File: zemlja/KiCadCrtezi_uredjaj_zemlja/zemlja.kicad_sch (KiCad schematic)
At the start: 24 parts, among them J1 AVR-ISP-6, J2 Barrel_Jack, J3 Arduino_ESP_Pin_Head_03x04, J4 Arduino_Analog_01x06_Socket, J5 Arduino_Pow_01x08_Socket, J6 Arduino_Pow_01x08_Socket, J7 Arduino_Digital_2_01x10_Socket, SW1 SW_Push, U1 TTL-RS485 Converter, U2 LCD 2x16 I2C, U3 7 in 1 Soil Sensor, U4 L7808

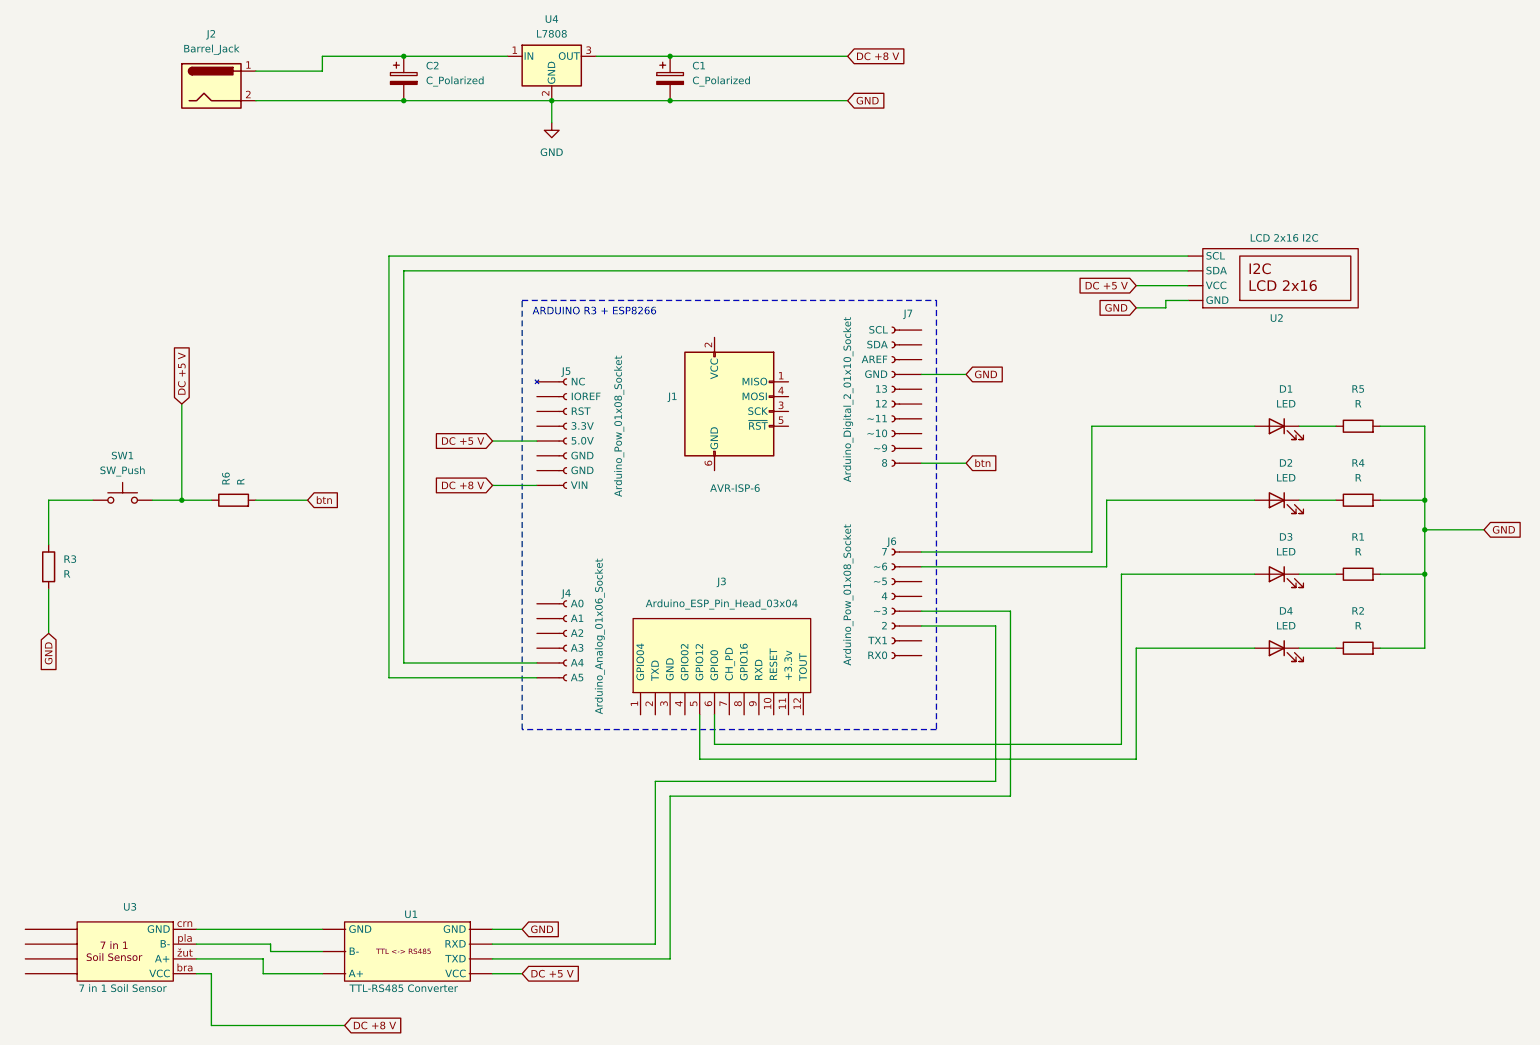
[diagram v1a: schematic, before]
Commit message: Na šemi uredđaja "zemlja" popravljene veze između kontrolnog dugmeta i uređaja. Popravljena i šema povezivanja dugmeta.
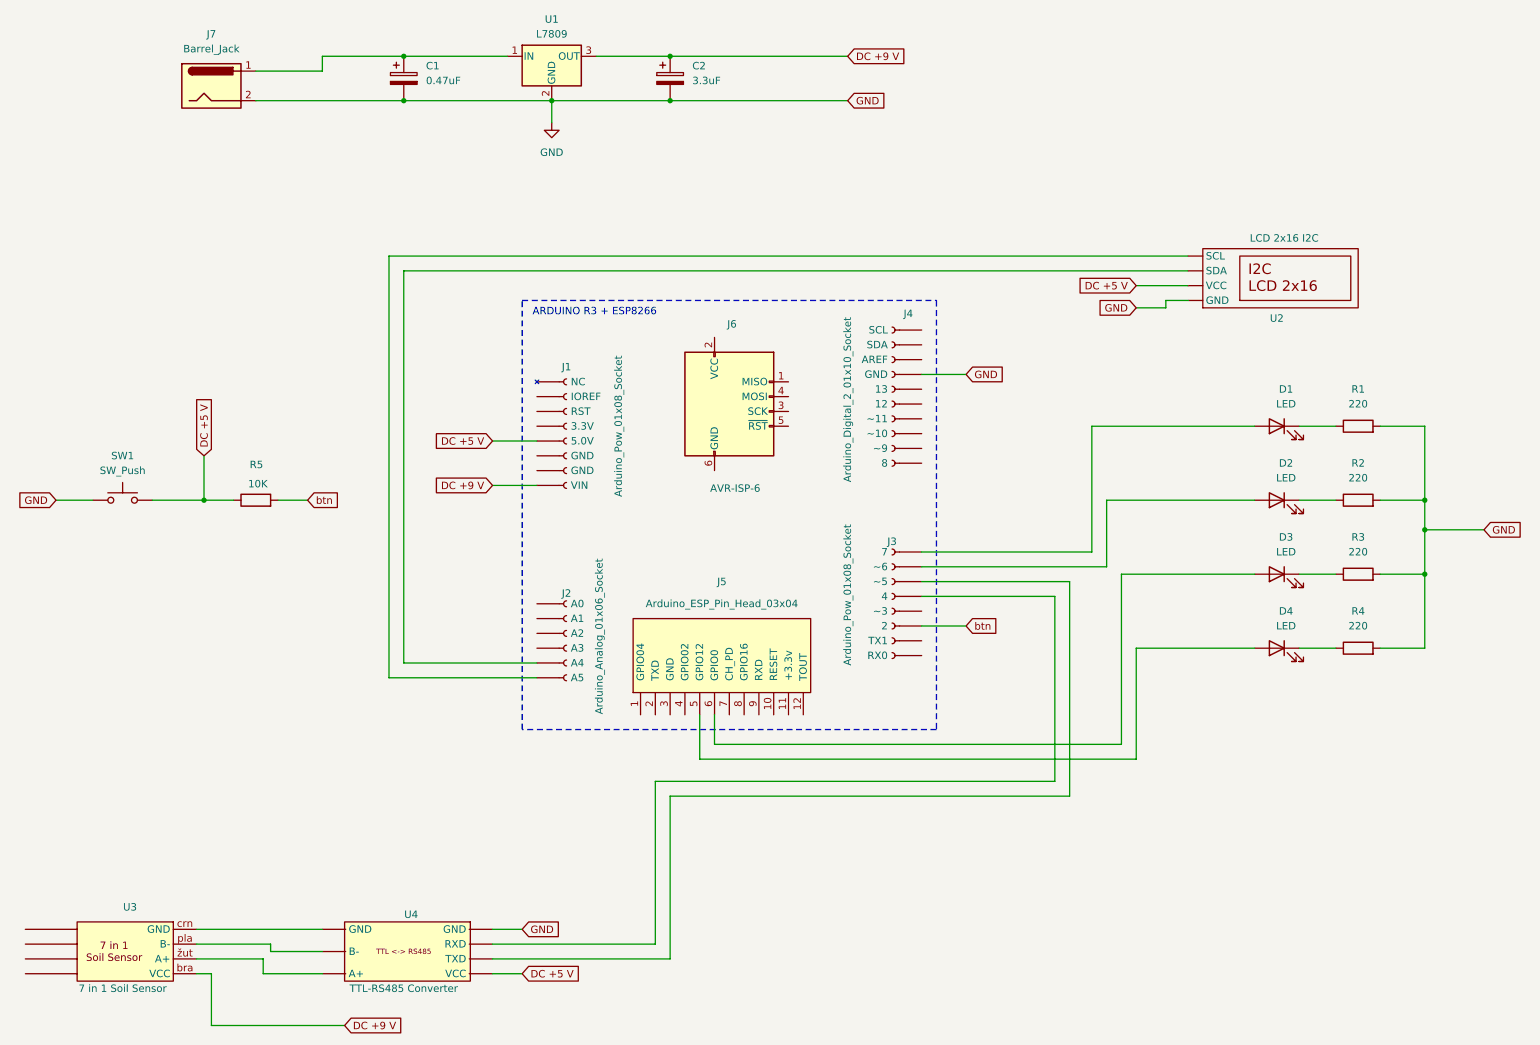
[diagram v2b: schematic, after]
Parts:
- removed R3: R, symbol Device:R
- removed U4: L7808, symbol Regulator_Linear:L7808
- added U1: L7809, symbol Regulator_Linear:L7809
- C1: renamed from C2; value C_Polarized -> 0.47uF
- C2: renamed from C1; value C_Polarized -> 3.3uF
- R1: renamed from R5; value R -> 220
- R2: renamed from R4; value R -> 220
- R3: renamed from R1; value R -> 220
- R4: renamed from R2; value R -> 220
- R5: renamed from R6; value R -> 10K
- renumbered J5 to J1, J4 to J2, J6 to J3, J7 to J4, J3 to J5, J1 to J6, J2 to J7, U1 to U4
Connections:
- net GND: now also SW1.1, U1.2 (GND)
- net btn: now also J3.6 (2); no longer J4.10 (8)
- net at C1.1, J7.1: now also U1.1 (IN)
- net at J3.3 (~5): now also U4. (VCC)
- net at J3.4: now also U4. (VCC)
- net at J3.5 (~3): no longer U4. (VCC)
- net DC +8 V renamed DC +9 V
- net DC +9 V: now also U1.3 (OUT)
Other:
- moved on the sheet: R5

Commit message: Na šemi uređaja zemla popravljene sve veze između led dioda i Arduino. Označene led diode po bojama.
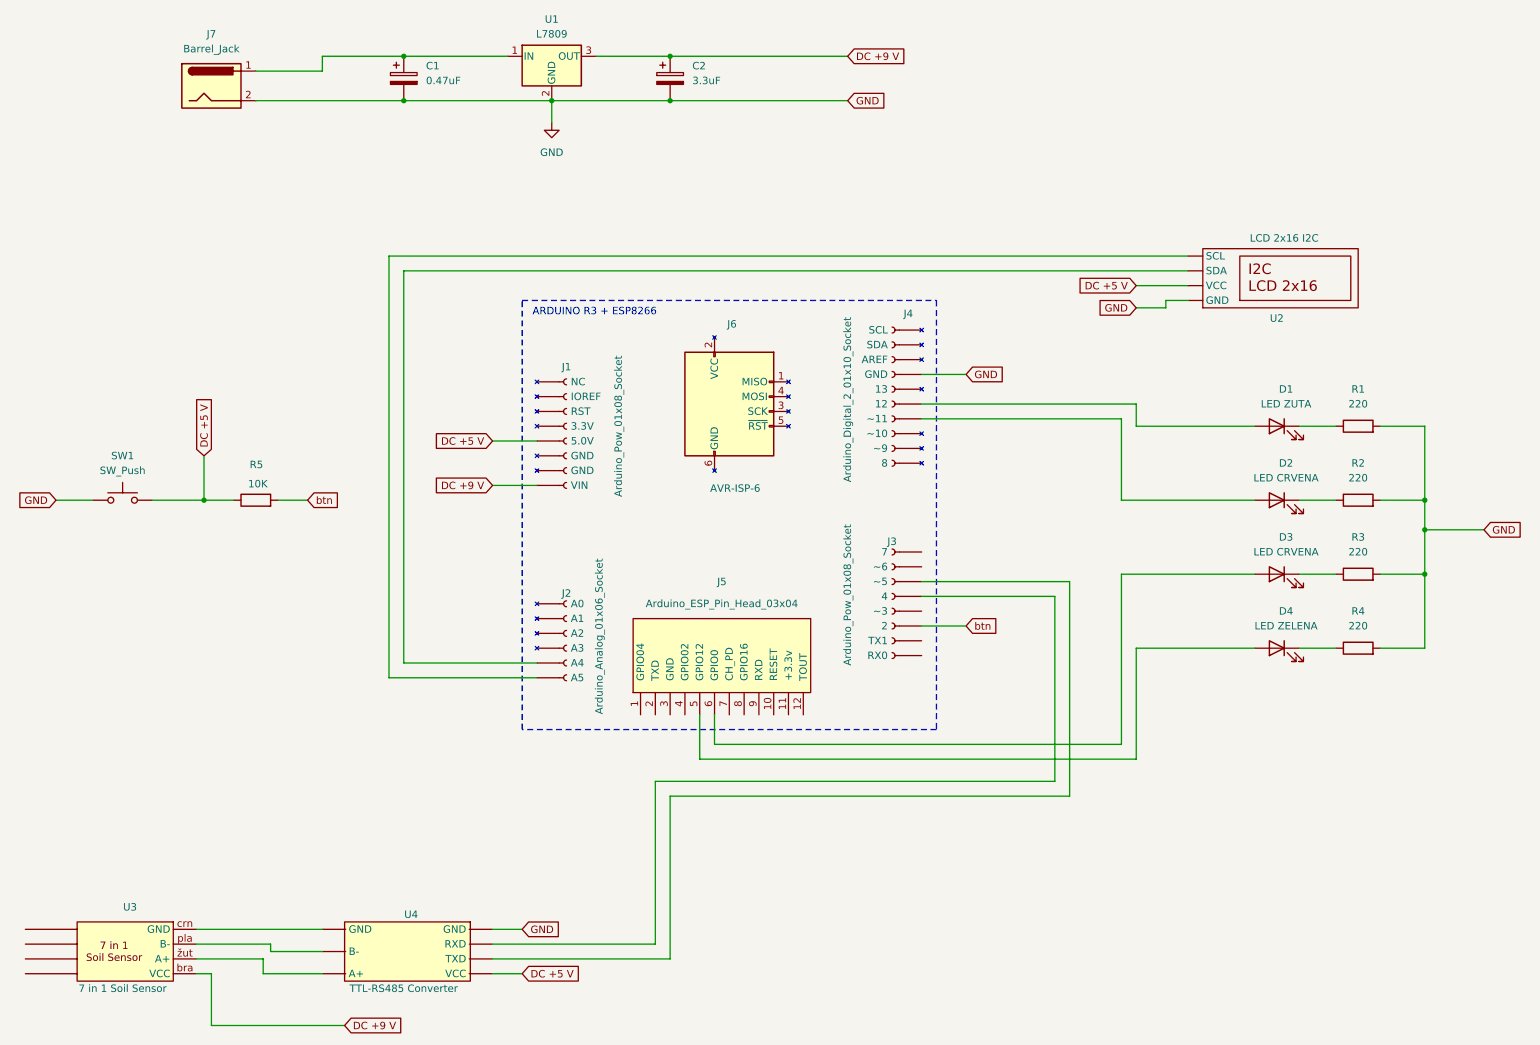
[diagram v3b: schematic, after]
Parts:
- D1: value LED -> LED ZUTA
- D2, D3: value LED -> LED CRVENA
- D4: value LED -> LED ZELENA
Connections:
- net at J4.6 (12): now also D1.2 (A)
- net at J4.7 (~11): now also D2.2 (A)
- net at J3.1 (7): no longer D1.2 (A)
- net at J3.2 (~6): no longer D2.2 (A)
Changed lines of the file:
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@@
 		(company "Poljoprivredna škola Bač")
 		(comment 1 "Izrađeno u sklopu projekta \"Pametna poljoprivreda\"")
-		(comment 2 "Licencirano sa GPL licencom")
+		(comment 2 "Licencirano sa GPL3 licencom")
 	)
 	(junction
@@
 	(wire
 		(pts
+			(xy 229.87 97.79) (xy 207.01 97.79)
+		)
+		(stroke
+			(width 0)
+			(type default)
+		)
+	)
+	(wire
+		(pts
 			(xy 259.08 85.09) (xy 259.08 97.79)
 		)
@@
 	(wire
 		(pts
+			(xy 209.55 81.28) (xy 172.72 81.28)
+		)
+		(stroke
+			(width 0)
+			(type default)
+		)
+	)
+	(wire
+		(pts
 			(xy 81.28 55.88) (xy 81.28 128.27)
 		)
@@
 	(wire
 		(pts
-			(xy 204.47 97.79) (xy 229.87 97.79)
+			(xy 207.01 97.79) (xy 207.01 83.82)
 		)
 		(stroke
@@
 	(wire
 		(pts
+			(xy 207.01 83.82) (xy 172.72 83.82)
+		)
+		(stroke
+			(width 0)
+			(type default)
+		)
+	)
+	(wire
+		(pts
 			(xy 58.42 24.13) (xy 69.85 24.13)
 		)
@@
 	(wire
 		(pts
-			(xy 172.72 109.22) (xy 204.47 109.22)
-		)
-		(stroke
-			(width 0)
-			(type default)
-		)
-	)
-	(wire
-		(pts
 			(xy 137.16 139.7) (xy 207.01 139.7)
 		)
@@
 	(wire
 		(pts
-			(xy 201.93 106.68) (xy 172.72 106.68)
-		)
-		(stroke
-			(width 0)
-			(type default)
-		)
-	)
-	(wire
-		(pts
-			(xy 229.87 85.09) (xy 201.93 85.09)
-		)
-		(stroke
-			(width 0)
-			(type default)
-		)
-	)
-	(wire
-		(pts
 			(xy 218.44 63.5) (xy 214.63 63.5)
 		)
@@
 	(wire
 		(pts
+			(xy 229.87 85.09) (xy 209.55 85.09)
+		)
+		(stroke
+			(width 0)
+			(type default)
+		)
+	)
+	(wire
+		(pts
 			(xy 134.62 134.62) (xy 134.62 142.24)
 		)
@@
 	(wire
 		(pts
-			(xy 201.93 85.09) (xy 201.93 106.68)
-		)
-		(stroke
-			(width 0)
-			(type default)
-		)
-	)
-	(wire
-		(pts
 			(xy 99.06 87.63) (xy 106.68 87.63)
 		)
@@
 	(wire
 		(pts
+			(xy 209.55 85.09) (xy 209.55 81.28)
+		)
+		(stroke
+			(width 0)
+			(type default)
+		)
+	)
+	(wire
+		(pts
 			(xy 129.54 148.59) (xy 198.12 148.59)
 		)
@@
 		(pts
 			(xy 251.46 85.09) (xy 259.08 85.09)
-		)
-		(stroke
-			(width 0)
-			(type default)
-		)
-	)
-	(wire
-		(pts
-			(xy 204.47 109.22) (xy 204.47 97.79)
 		)
 		(stroke
@@
 			)
 		)
-		(property "Value" "LED"
+		(property "Value" "LED ZELENA"
 			(at 235.2675 119.38 0)
 			(effects
@@
 		(property "Reference" "J1"
 			(at 111.76 74.168 0)
-			(do_not_autoplace yes)
 			(effects
 				(font
@@
 		(property "Value" "Arduino_Pow_01x08_Socket"
 			(at 121.412 85.09 90)
-			(do_not_autoplace yes)
 			(effects
 				(font
@@
 			)
 		)
-		(property "Value" "LED"
+		(property "Value" "LED CRVENA"
 			(at 235.2675 106.68 0)
 			(effects
@@
 		(property "Reference" "J4"
 			(at 170.434 65.024 0)
-			(do_not_autoplace yes)
 			(effects
 				(font
@@
 		(property "Value" "Arduino_Digital_2_01x10_Socket"
 			(at 159.258 80.518 90)
-			(do_not_autoplace yes)
 			(effects
 				(font
@@
 			)
 		)
-		(property "Value" "LED"
+		(property "Value" "LED ZUTA"
 			(at 235.2675 81.28 0)
 			(effects
@@
 			)
 		)
-		(property "Value" "LED"
+		(property "Value" "LED CRVENA"
 			(at 235.2675 93.98 0)
 			(effects
@@
 		(property "Reference" "J2"
 			(at 111.76 113.03 0)
-			(do_not_autoplace yes)
 			(effects
 				(font
@@
 		(property "Value" "Arduino_Analog_01x06_Socket"
 			(at 118.11 121.158 90)
-			(do_not_autoplace yes)
 			(effects
 				(font
@@
 		(property "Reference" "U4"
 			(at 85.09 168.91 0)
-			(do_not_autoplace yes)
 			(effects
 				(font
@@
 		(property "Value" "TTL-RS485 Converter"
 			(at 83.82 181.61 0)
-			(do_not_autoplace yes)
-			(effects
-				(font
+			(effects
+				(font
